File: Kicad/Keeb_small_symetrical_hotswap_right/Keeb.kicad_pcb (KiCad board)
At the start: 2 copper layers, 96.2 x 98.1 mm, 32 parts, among them J2 B2B-XH-A_LF__SN_, J3 MJ-4PP-9_MJ-4PP-9, SW1 CherryMX, SW10 CherryMX, SW11 CherryMX, SW13 CherryMX, SW14 CherryMX, SW15 CherryMX, SW16 CherryMX, SW17 CherryMX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

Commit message: Initial commit
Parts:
- removed SW2: CherryMX, ScottoKeebs_Hotswap:Hotswap_MX_Plated_1.00u
- removed U1: Pico, MCU_RaspberryPi_and_Boards:RPi_Pico_SMD_TH_NO_BACK_HOLES
- added U3: nice_nano, Nice_nano:nice_nano, F.Cu at (172.7, 112.0)
- J3: footprint MJ-4PP-9:MJ-4PP-9_no_silk -> MJ-4PP-9:MJ-4PP-9
- turned J3 to -90 degrees
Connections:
- J3 pad 3: 15 -> 10
- J3 pad 4: 14 -> 10
- SW1 pad 1: 3 -> GND
- SW1 pad 2: GND -> 21
- SW10 pad 1: 17 -> 8
- SW11 pad 1: 16 -> 7
- SW14 pad 2: 10 -> 14
- SW15 pad 2: 11 -> 15
- SW16 pad 1: 4 -> 20
- SW17 pad 2: 12 -> 16
- SW18 pad 2: 5 -> 17
- SW19 pad 2: 1 -> 18
- SW20 pad 2: 0 -> 19
- SW3 pad 1: GND -> 2
- SW3 pad 2: 26 -> GND
- SW4 pad 1: GND -> 3
- SW4 pad 2: 27 -> GND
- SW5 pad 1: 28 -> 1
- SW6 pad 1: 19 -> 6
- SW7 pad 1: 20 -> 5
- SW8 pad 1: 21 -> 4
- SW9 pad 1: 18 -> 9
- U2 pad CLK: 8 -> 12
- U2 pad DT: 9 -> 11
- U2 pad SW: 2 -> unconnected-(U2-PadSW)
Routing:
- net 16: track 13.7 -> 91.7 mm
- net 22: track 77.8 -> 0.00 mm
- net 2: track 137.8 -> 62.9 mm
- net 0: track 74.8 -> 0.00 mm
- net 3v3: track 243.5 -> 170.2 mm
- net GND: track 544.1 -> 612.3 mm
- net 11: track 37.5 -> 103.0 mm
- net 6: track 0.00 -> 65.0 mm
- net 26: track 63.8 -> 0.00 mm
- net 3: track 34.4 -> 95.0 mm
- net 8: track 113.4 -> 58.6 mm
- net 27: track 44.7 -> 0.00 mm
- net 5: track 88.0 -> 46.7 mm
- net 7: track 0.00 -> 39.7 mm
- net 17: track 36.5 -> 75.7 mm
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
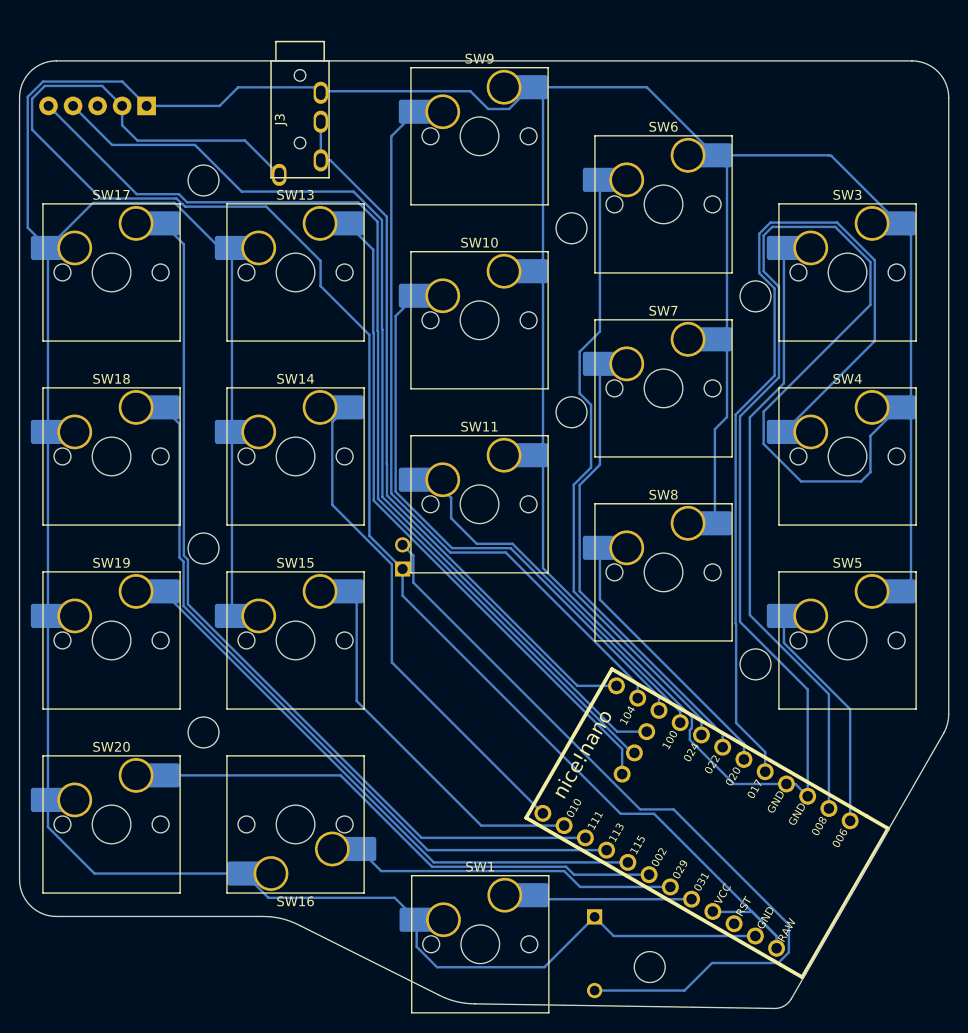
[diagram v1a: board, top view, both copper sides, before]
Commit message: current version, all problems fixed, software compiled for CP 9.0
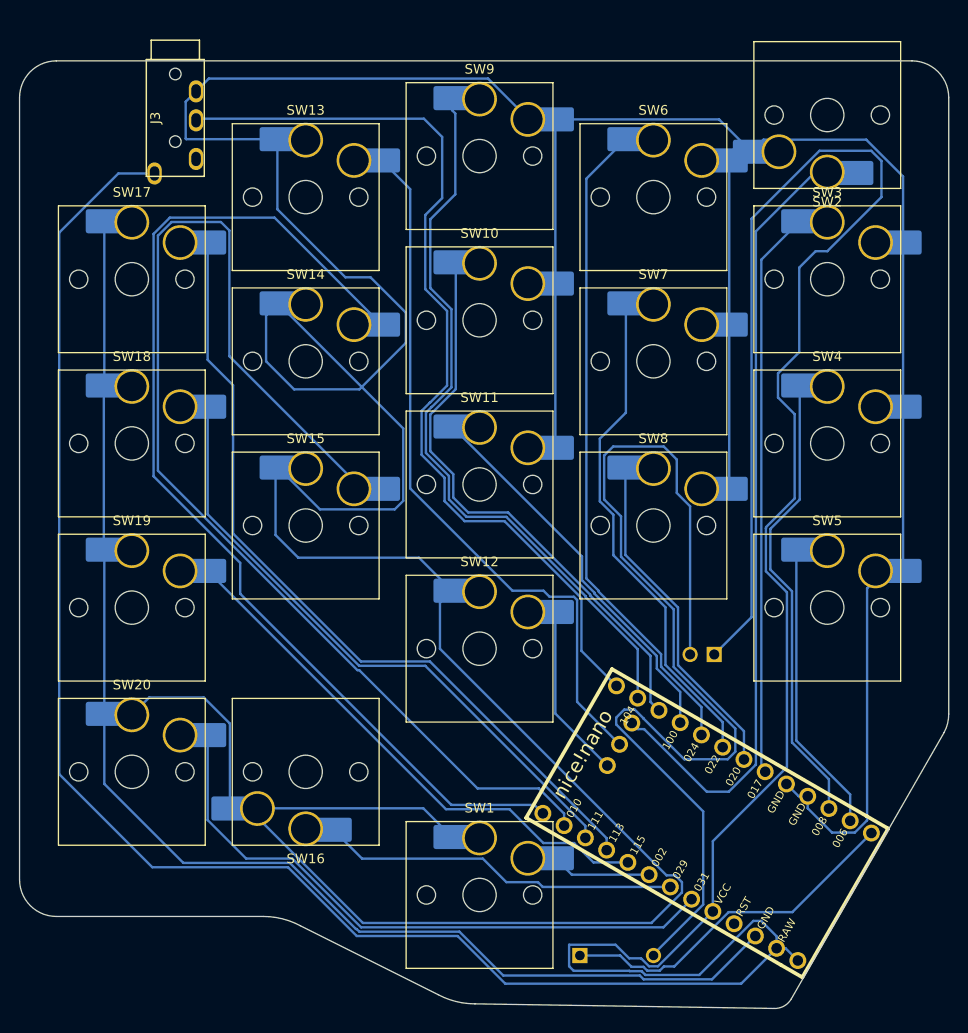
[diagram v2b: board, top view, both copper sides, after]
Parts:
- removed H1, H2, H3, H4, H5, H7, H8, H9: MountingHole, MountingHole:MountingHole_3.2mm_M3
- removed U2: KY-040, KY-040:KY-040-PORT
- added SW12: CherryMX, ScottoKeebs_Hotswap:Hotswap_Choc_V1_Plated_1.00u, F.Cu at (150.2, 94.6)
- added SW2: CherryMX, ScottoKeebs_Hotswap:Hotswap_Choc_V1_Plated_1.00u, F.Cu at (186.2, 39.3)
- SW1, SW10, SW11, SW13, SW14, SW15, SW16, SW17, SW18, SW19, SW20, SW3, SW4, SW5, SW6, SW7, SW8, SW9: footprint ScottoKeebs_Hotswap:Hotswap_MX_Plated_1.00u -> ScottoKeebs_Hotswap:Hotswap_Choc_V1_Plated_1.00u
- moved J2 33.3 mm to (173.3, 95.7), turned to 0 degrees
- moved J3 12.9 mm to (118.8, 39.6)
- moved SW15 11.9 mm to (132.2, 81.8)
- moved SW14 9.91 mm to (132.2, 64.8)
- moved SW13 7.87 mm to (132.2, 47.8)
- moved SW20 5.84 mm to (114.2, 107.3)
- moved SW16 5.55 mm to (132.2, 107.3)
- moved SW1 5.11 mm to (150.2, 120.1)
- moved SW8 4.96 mm to (168.2, 81.8)
- moved SW19 4.00 mm to (114.2, 90.3)
- moved SW5 4.00 mm to (186.2, 90.3)
- moved SW7 2.99 mm to (168.2, 64.8)
- moved SW18 2.50 mm to (114.2, 73.3)
- moved SW4 2.50 mm to (186.2, 73.3)
- moved S1 2.29 mm to (164.4, 126.3), turned to 90 degrees
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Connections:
- J3 pad 4: 10 -> unconnected-(J3-D-Pad4)
- S1 pad 1A: GND -> B-
- SW1 pad 2: 21 -> 19
- SW13 pad 2: 13 -> 12
- SW17 pad 2: 16 -> 17
- SW18 pad 2: 17 -> 16
- SW20 pad 2: 19 -> 21
- SW3 pad 1: 2 -> 3
- SW4 pad 1: 3 -> 2
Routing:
- net 3v3: track 170.2 -> 354.8 mm
- net 15: track 38.6 -> 125.1 mm
- net 14: track 51.7 -> 110.6 mm
- net 13: track 68.8 -> 18.1 mm
- net 21: track 16.7 -> 64.7 mm
- net 19: track 54.6 -> 10.4 mm
- net B-: track 0.00 -> 36.7 mm
- net 3: track 95.0 -> 58.8 mm
- net 12: track 105.2 -> 74.0 mm
- net Net-(J2-Pad2): track 82.5 -> 111.1 mm
- net GND: track 612.3 -> 640.4 mm
- net 16: track 91.7 -> 64.8 mm
- net 10: track 74.0 -> 96.7 mm
- net 11: track 103.0 -> 84.9 mm
- net 2: track 62.9 -> 47.6 mm
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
